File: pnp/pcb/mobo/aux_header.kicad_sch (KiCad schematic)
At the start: 1 part, among them J20 AUX1

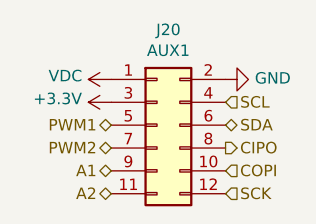
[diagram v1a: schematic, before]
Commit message: Connect all sub-sheets together
Refactored schematic is checked against existing lay-out.
Connectivity has stayed the same.
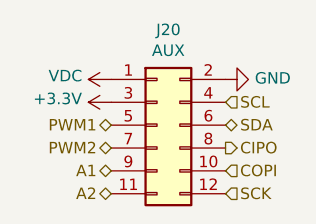
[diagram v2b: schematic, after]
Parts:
- J20: value AUX1 -> AUX
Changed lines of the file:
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@@
     (in_bom yes) (on_board yes)
     (property "Reference" "J20" (id 0) (at 144.78 86.5632 0))
-    (property "Value" "AUX1" (id 1) (at 144.78 88.8746 0))
+    (property "Value" "AUX" (id 1) (at 144.78 88.8746 0))
     (property "Footprint" "Connector_IDC:IDC-Header_2x06_P2.54mm_Vertical" (id 2) (at 143.51 97.155 0)
       (effects (font (size 1.27 1.27)) hide)

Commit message: Fixed schematic parity
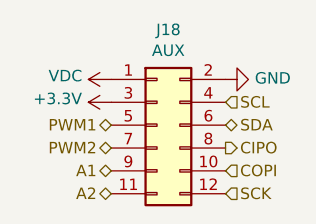
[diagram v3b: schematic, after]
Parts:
- renumbered J20 to J18
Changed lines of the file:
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@@
     (effects (font (size 1.27 1.27)) (justify left))
   )
-  (symbol (lib_id "power:GND") (at 151.13 92.075 90)
+  (symbol (lib_id "power:GND") (at 151.13 92.075 90) (unit 1)
     (in_bom yes) (on_board yes)
-    (property "Reference" "#PWR0238" (id 0) (at 157.48 92.075 0)
+    (property "Reference" "#PWR0232" (id 0) (at 157.48 92.075 0)
       (effects (font (size 1.27 1.27)) hide)
     )
@@
     (pin "1")
   )
-  (symbol (lib_id "power:VDC") (at 138.43 92.075 90)
+  (symbol (lib_id "power:VDC") (at 138.43 92.075 90) (unit 1)
     (in_bom yes) (on_board yes)
-    (property "Reference" "#PWR0236" (id 0) (at 140.97 92.075 0)
+    (property "Reference" "#PWR0230" (id 0) (at 140.97 92.075 0)
       (effects (font (size 1.27 1.27)) hide)
     )
@@
     (pin "1")
   )
-  (symbol (lib_id "Connector_Generic:Conn_02x06_Odd_Even") (at 143.51 97.155 0)
+  (symbol (lib_id "Connector_Generic:Conn_02x06_Odd_Even") (at 143.51 97.155 0) (unit 1)
     (in_bom yes) (on_board yes)
-    (property "Reference" "J20" (id 0) (at 144.78 86.5632 0))
+    (property "Reference" "J18" (id 0) (at 144.78 86.5632 0))
     (property "Value" "AUX" (id 1) (at 144.78 88.8746 0))
     (property "Footprint" "Connector_IDC:IDC-Header_2x06_P2.54mm_Vertical" (id 2) (at 143.51 97.155 0)
@@
     (pin "9")
   )
-  (symbol (lib_id "power:+3.3V") (at 138.43 94.615 90)
+  (symbol (lib_id "power:+3.3V") (at 138.43 94.615 90) (unit 1)
     (in_bom yes) (on_board yes)
-    (property "Reference" "#PWR0237" (id 0) (at 142.24 94.615 0)
+    (property "Reference" "#PWR0231" (id 0) (at 142.24 94.615 0)
       (effects (font (size 1.27 1.27)) hide)
     )

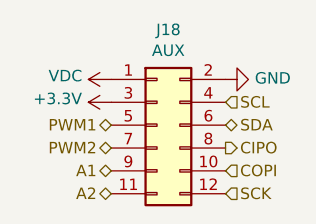
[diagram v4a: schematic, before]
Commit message: moving mobo-rev04b0 into mobo-rev04 branch from old repo
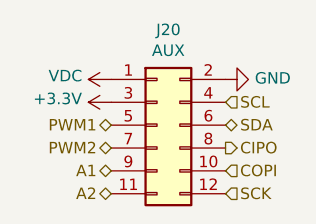
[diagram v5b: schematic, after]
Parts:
- renumbered J18 to J20
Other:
- company: (none) -> Opulo
- title: (none) -> LumenPnP Motherboard
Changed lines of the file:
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@@
   (paper "A4")
   (title_block
+    (title "LumenPnP Motherboard")
     (date "2022-03-29")
+    (company "Opulo")
   )
   (hierarchical_label "PWM1" (shape bidirectional) (at 138.43 97.155 180)
@@
     (effects (font (size 1.27 1.27)) (justify left))
   )
-  (symbol (lib_id "power:GND") (at 151.13 92.075 90) (unit 1)
+  (symbol (lib_id "power:GND") (at 151.13 92.075 90)
     (in_bom yes) (on_board yes)
-    (property "Reference" "#PWR0232" (id 0) (at 157.48 92.075 0)
+    (property "Reference" "#PWR0238" (id 0) (at 157.48 92.075 0)
       (effects (font (size 1.27 1.27)) hide)
     )
@@
     (pin "1")
   )
-  (symbol (lib_id "power:VDC") (at 138.43 92.075 90) (unit 1)
+  (symbol (lib_id "power:VDC") (at 138.43 92.075 90)
     (in_bom yes) (on_board yes)
-    (property "Reference" "#PWR0230" (id 0) (at 140.97 92.075 0)
+    (property "Reference" "#PWR0236" (id 0) (at 140.97 92.075 0)
       (effects (font (size 1.27 1.27)) hide)
     )
@@
     (pin "1")
   )
-  (symbol (lib_id "Connector_Generic:Conn_02x06_Odd_Even") (at 143.51 97.155 0) (unit 1)
+  (symbol (lib_id "Connector_Generic:Conn_02x06_Odd_Even") (at 143.51 97.155 0)
     (in_bom yes) (on_board yes)
-    (property "Reference" "J18" (id 0) (at 144.78 86.5632 0))
+    (property "Reference" "J20" (id 0) (at 144.78 86.5632 0))
     (property "Value" "AUX" (id 1) (at 144.78 88.8746 0))
     (property "Footprint" "Connector_IDC:IDC-Header_2x06_P2.54mm_Vertical" (id 2) (at 143.51 97.155 0)
@@
     (pin "9")
   )
-  (symbol (lib_id "power:+3.3V") (at 138.43 94.615 90) (unit 1)
+  (symbol (lib_id "power:+3.3V") (at 138.43 94.615 90)
     (in_bom yes) (on_board yes)
-    (property "Reference" "#PWR0231" (id 0) (at 142.24 94.615 0)
+    (property "Reference" "#PWR0237" (id 0) (at 142.24 94.615 0)
       (effects (font (size 1.27 1.27)) hide)
     )

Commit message: Update mobo schematic with part numbers and ratings
All parts now have part numbers for at least one reseller or manufacturer along with rating specifications.

Note: I did not update the PCB with these new properties, as it seems the PCB is a bit out of sync with the schematic.
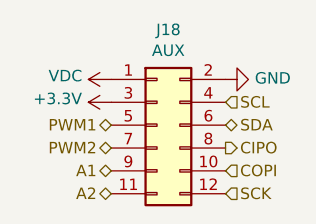
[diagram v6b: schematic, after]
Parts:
- renumbered J20 to J18
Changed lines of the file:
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@@
-(kicad_sch (version 20211123) (generator eeschema)
+(kicad_sch (version 20230121) (generator eeschema)
   (paper "A4")
   (title_block
@@
     (company "Opulo")
   )
-  (hierarchical_label "PWM1" (shape bidirectional) (at 138.43 97.155 180)
+  (hierarchical_label "PWM1" (shape bidirectional) (at 138.43 97.155 180) (fields_autoplaced)
     (effects (font (size 1.27 1.27)) (justify right))
   )
-  (hierarchical_label "A2" (shape bidirectional) (at 138.43 104.775 180)
+  (hierarchical_label "A2" (shape bidirectional) (at 138.43 104.775 180) (fields_autoplaced)
     (effects (font (size 1.27 1.27)) (justify right))
   )
-  (hierarchical_label "COPI" (shape input) (at 151.13 102.235 0)
+  (hierarchical_label "COPI" (shape input) (at 151.13 102.235 0) (fields_autoplaced)
     (effects (font (size 1.27 1.27)) (justify left))
   )
-  (hierarchical_label "A1" (shape bidirectional) (at 138.43 102.235 180)
+  (hierarchical_label "A1" (shape bidirectional) (at 138.43 102.235 180) (fields_autoplaced)
     (effects (font (size 1.27 1.27)) (justify right))
   )
-  (hierarchical_label "CIPO" (shape output) (at 151.13 99.695 0)
+  (hierarchical_label "CIPO" (shape output) (at 151.13 99.695 0) (fields_autoplaced)
     (effects (font (size 1.27 1.27)) (justify left))
   )
-  (hierarchical_label "PWM2" (shape bidirectional) (at 138.43 99.695 180)
+  (hierarchical_label "PWM2" (shape bidirectional) (at 138.43 99.695 180) (fields_autoplaced)
     (effects (font (size 1.27 1.27)) (justify right))
   )
-  (hierarchical_label "SCL" (shape input) (at 151.13 94.615 0)
+  (hierarchical_label "SCL" (shape input) (at 151.13 94.615 0) (fields_autoplaced)
     (effects (font (size 1.27 1.27)) (justify left))
   )
-  (hierarchical_label "SCK" (shape input) (at 151.13 104.775 0)
+  (hierarchical_label "SCK" (shape input) (at 151.13 104.775 0) (fields_autoplaced)
     (effects (font (size 1.27 1.27)) (justify left))
   )
-  (hierarchical_label "SDA" (shape bidirectional) (at 151.13 97.155 0)
+  (hierarchical_label "SDA" (shape bidirectional) (at 151.13 97.155 0) (fields_autoplaced)
     (effects (font (size 1.27 1.27)) (justify left))
   )
-  (symbol (lib_id "power:GND") (at 151.13 92.075 90)
-    (in_bom yes) (on_board yes)
-    (property "Reference" "#PWR0238" (id 0) (at 157.48 92.075 0)
+  (symbol (lib_id "power:GND") (at 151.13 92.075 90) (unit 1)
+    (in_bom yes) (on_board yes) (dnp no)
+    (property "Reference" "#PWR0232" (at 157.48 92.075 0)
       (effects (font (size 1.27 1.27)) hide)
     )
-    (property "Value" "GND" (id 1) (at 154.3812 91.948 90)
+    (property "Value" "GND" (at 154.3812 91.948 90)
       (effects (font (size 1.27 1.27)) (justify right))
     )
-    (property "Footprint" "" (id 2) (at 151.13 92.075 0)
+    (property "Footprint" "" (at 151.13 92.075 0)
       (effects (font (size 1.27 1.27)) hide)
     )
-    (property "Datasheet" "" (id 3) (at 151.13 92.075 0)
+    (property "Datasheet" "" (at 151.13 92.075 0)
       (effects (font (size 1.27 1.27)) hide)
     )
     (pin "1")
+    (instances
+      (project "mobo"
+        (path "/7255cbd1-8d38-4545-be9a-7fc5488ef942/00000000-0000-0000-0000-00005eb0c492/315eaff0-1b3b-44a6-ac69-840413dbfa19"
+          (reference "#PWR0232") (unit 1)
+        )
+        (path "/7255cbd1-8d38-4545-be9a-7fc5488ef942/00000000-0000-0000-0000-00005eb0c492/e879fa5c-c0d9-49d4-804e-02baaa1a0697"
+          (reference "#PWR0235") (unit 1)
+        )
+        (path "/7255cbd1-8d38-4545-be9a-7fc5488ef942/00000000-0000-0000-0000-00005eb0c492/cdb39402-8548-471b-84fd-7e7ff4d5b5c8"
+          (reference "#PWR0238") (unit 1)
+        )
+      )
+    )
   )
-  (symbol (lib_id "power:VDC") (at 138.43 92.075 90)
-    (in_bom yes) (on_board yes)
-    (property "Reference" "#PWR0236" (id 0) (at 140.97 92.075 0)
+  (symbol (lib_id "power:VDC") (at 138.43 92.075 90) (unit 1)
+    (in_bom yes) (on_board yes) (dnp no)
+    (property "Reference" "#PWR0230" (at 140.97 92.075 0)
       (effects (font (size 1.27 1.27)) hide)
     )
-    (property "Value" "VDC" (id 1) (at 135.2042 91.694 90)
+    (property "Value" "VDC" (at 135.2042 91.694 90)
       (effects (font (size 1.27 1.27)) (justify left))
     )
-    (property "Footprint" "" (id 2) (at 138.43 92.075 0)
+    (property "Footprint" "" (at 138.43 92.075 0)
       (effects (font (size 1.27 1.27)) hide)
     )
-    (property "Datasheet" "" (id 3) (at 138.43 92.075 0)
+    (property "Datasheet" "" (at 138.43 92.075 0)
       (effects (font (size 1.27 1.27)) hide)
     )
     (pin "1")
+    (instances
+      (project "mobo"
+        (path "/7255cbd1-8d38-4545-be9a-7fc5488ef942/00000000-0000-0000-0000-00005eb0c492/315eaff0-1b3b-44a6-ac69-840413dbfa19"
+          (reference "#PWR0230") (unit 1)
+        )
+        (path "/7255cbd1-8d38-4545-be9a-7fc5488ef942/00000000-0000-0000-0000-00005eb0c492/e879fa5c-c0d9-49d4-804e-02baaa1a0697"
+          (reference "#PWR0233") (unit 1)
+        )
+        (path "/7255cbd1-8d38-4545-be9a-7fc5488ef942/00000000-0000-0000-0000-00005eb0c492/cdb39402-8548-471b-84fd-7e7ff4d5b5c8"
+          (reference "#PWR0236") (unit 1)
+        )
+      )
+    )
   )
-  (symbol (lib_id "Connector_Generic:Conn_02x06_Odd_Even") (at 143.51 97.155 0)
-    (in_bom yes) (on_board yes)
-    (property "Reference" "J20" (id 0) (at 144.78 86.5632 0))
-    (property "Value" "AUX" (id 1) (at 144.78 88.8746 0))
-    (property "Footprint" "Connector_IDC:IDC-Header_2x06_P2.54mm_Vertical" (id 2) (at 143.51 97.155 0)
+  (symbol (lib_id "Connector_Generic:Conn_02x06_Odd_Even") (at 143.51 97.155 0) (unit 1)
+    (in_bom yes) (on_board yes) (dnp no)
+    (property "Reference" "J18" (at 144.78 86.5632 0)
+      (effects (font (size 1.27 1.27)))
+    )
+    (property "Value" "AUX" (at 144.78 88.8746 0)
+      (effects (font (size 1.27 1.27)))
+    )
+    (property "Footprint" "Connector_IDC:IDC-Header_2x06_P2.54mm_Vertical" (at 143.51 97.155 0)
       (effects (font (size 1.27 1.27)) hide)
     )
-    (property "Datasheet" "~" (id 3) (at 143.51 97.155 0)
+    (property "Datasheet" "~" (at 143.51 97.155 0)
       (effects (font (size 1.27 1.27)) hide)
     )
-    (property "LCSC" "C9136" (id 4) (at 143.51 97.155 0)
+    (property "LCSC" "C9136" (at 143.51 97.155 0)
       (effects (font (size 1.27 1.27)) hide)
     )
@@
     (pin "8")
     (pin "9")
+    (instances
+      (project "mobo"
+        (path "/7255cbd1-8d38-4545-be9a-7fc5488ef942/00000000-0000-0000-0000-00005eb0c492/315eaff0-1b3b-44a6-ac69-840413dbfa19"
+          (reference "J18") (unit 1)
+        )
+        (path "/7255cbd1-8d38-4545-be9a-7fc5488ef942/00000000-0000-0000-0000-00005eb0c492/e879fa5c-c0d9-49d4-804e-02baaa1a0697"
+          (reference "J19") (unit 1)
+        )
+        (path "/7255cbd1-8d38-4545-be9a-7fc5488ef942/00000000-0000-0000-0000-00005eb0c492/cdb39402-8548-471b-84fd-7e7ff4d5b5c8"
+          (reference "J20") (unit 1)
+        )
+      )
+    )
   )
-  (symbol (lib_id "power:+3.3V") (at 138.43 94.615 90)
-    (in_bom yes) (on_board yes)
-    (property "Reference" "#PWR0237" (id 0) (at 142.24 94.615 0)
+  (symbol (lib_id "power:+3.3V") (at 138.43 94.615 90) (unit 1)
+    (in_bom yes) (on_board yes) (dnp no)
+    (property "Reference" "#PWR0231" (at 142.24 94.615 0)
       (effects (font (size 1.27 1.27)) hide)
     )
-    (property "Value" "+3.3V" (id 1) (at 135.1788 94.234 90)
+    (property "Value" "+3.3V" (at 135.1788 94.234 90)
       (effects (font (size 1.27 1.27)) (justify left))
     )
-    (property "Footprint" "" (id 2) (at 138.43 94.615 0)
+    (property "Footprint" "" (at 138.43 94.615 0)
       (effects (font (size 1.27 1.27)) hide)
     )
-    (property "Datasheet" "" (id 3) (at 138.43 94.615 0)
+    (property "Datasheet" "" (at 138.43 94.615 0)
       (effects (font (size 1.27 1.27)) hide)
     )
     (pin "1")
+    (instances
+      (project "mobo"
+        (path "/7255cbd1-8d38-4545-be9a-7fc5488ef942/00000000-0000-0000-0000-00005eb0c492/315eaff0-1b3b-44a6-ac69-840413dbfa19"
+          (reference "#PWR0231") (unit 1)
+        )
+        (path "/7255cbd1-8d38-4545-be9a-7fc5488ef942/00000000-0000-0000-0000-00005eb0c492/e879fa5c-c0d9-49d4-804e-02baaa1a0697"
+          (reference "#PWR0234") (unit 1)
+        )
+        (path "/7255cbd1-8d38-4545-be9a-7fc5488ef942/00000000-0000-0000-0000-00005eb0c492/cdb39402-8548-471b-84fd-7e7ff4d5b5c8"
+          (reference "#PWR0237") (unit 1)
+        )
+      )
+    )
   )
 )
